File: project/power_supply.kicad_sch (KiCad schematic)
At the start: 0 parts

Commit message: Regulador V1 finalizado
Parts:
- added C1, C2, C3: 2u2, symbol Device:C
- added D1: ~, Package_TO_SOT_SMD:SOT-23, symbol Diode:MMBZxx
- added D2: LED, symbol Device:LED
- added FB1, FB2, FB3: FerriteBead_Small, symbol Device:FerriteBead_Small
- added J1: USB_C_Receptacle_USB2.0_16P, symbol Connector:USB_C_Receptacle_USB2.0_16P
- added R1, R2: 5k1, symbol Device:R
- added R3: 1k, symbol Device:R
- added TP1_5V, TP2_3V3, TP3_1V2: TestPoint, symbol Connector:TestPoint
- added U1: USBLC6-2SC6, Package_TO_SOT_SMD:SOT-23-6, symbol Power_Protection:USBLC6-2SC6
- added U2: MIC5356-S4YMME, Package_SO:MSOP-8-1EP_3x3mm_P0.65mm_EP2.5x3mm_Mask1.73x2.36mm_ThermalVias, symbol Regulator_Linear:MIC5356-S4YMME
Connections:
- new net: D1.1 (K), D1.2 (K), FB1.1, J1.A4 (VBUS), J1.A9 (VBUS), J1.B4 (VBUS), J1.B9 (VBUS), U1.5 (VBUS)
- new net: D2.2 (A), R3.2
- new net: FB3.1, U2.7 (VOUT2)
- new net: FB2.1, U2.8 (VOUT1)
- new net: J1.A5 (CC1), R1.1
- new net: J1.A6 (D+), J1.B6 (D+), U1.3 (I/O2)
- new net: J1.A7 (D-), J1.B7 (D-), U1.1 (I/O1)
- new net: J1.B5 (CC2), R2.1
- new net +1V2: C2.1, FB3.2, TP3_1V2.1
- new net +3V3: C3.1, FB2.2, TP2_3V3.1
- new net +5V: C1.1, FB1.2, R3.1, TP1_5V.1, U2.1 (VIN), U2.4 (EN2), U2.5 (EN1)
- new net D+: U1.4 (I/O2)
- new net D-: U1.6 (I/O1)
- new net GND: C1.2, C2.2, C3.2, D1.3 (A), D2.1 (K), J1.A1 (GND), J1.A12 (GND), J1.B1 (GND), J1.B12 (GND), J1.S1 (SHIELD), R1.2, R2.2, U1.2 (GND), U2.2 (GND)
- no-connect marks 0 -> 2

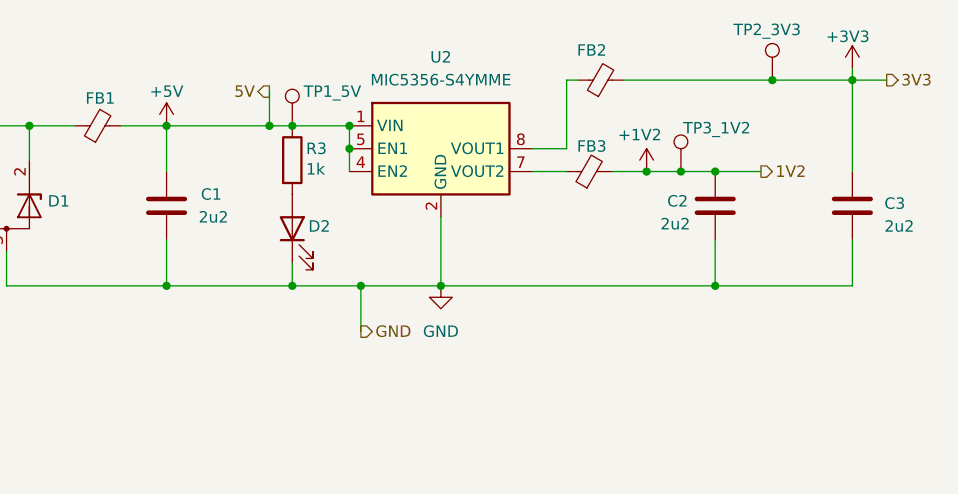
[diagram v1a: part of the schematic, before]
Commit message: Sección de FTDI casi terminada. Definir oscilador y nombres de puertos
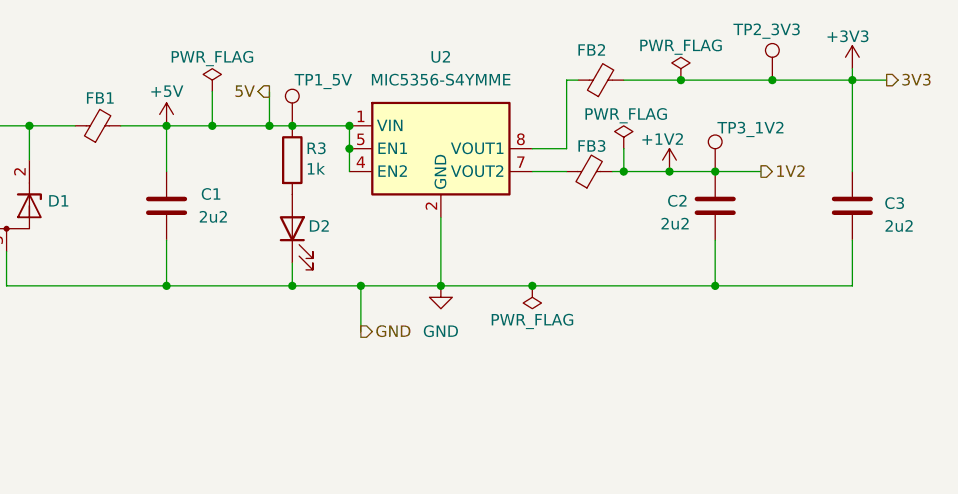
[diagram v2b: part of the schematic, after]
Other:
- moved on the sheet: TP3_1V2

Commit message: Guardado previo, FTDI casi listo
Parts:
- removed TP1_5V, TP2_3V3, TP3_1V2: TestPoint, symbol Connector:TestPoint
- removed U1: USBLC6-2SC6, Package_TO_SOT_SMD:SOT-23-6, symbol Power_Protection:USBLC6-2SC6
- removed U2: MIC5356-S4YMME, Package_SO:MSOP-8-1EP_3x3mm_P0.65mm_EP2.5x3mm_Mask1.73x2.36mm_ThermalVias, symbol Regulator_Linear:MIC5356-S4YMME
- added C4, C6, C7: 10u, symbol Device:C
- added C5: 100n, symbol Device:C
- added R4: 120, symbol Device:R
- added TP1: TP2_3V1, symbol Connector:TestPoint
- added TP2: TP1_5V1, symbol Connector:TestPoint
- added TP3: TP3_1V2, symbol Connector:TestPoint
- added TP4: TP4_GND, symbol Connector:TestPoint
- added U1: LD1117S33TR_SOT223, Package_TO_SOT_SMD:SOT-223-3_TabPin2, symbol Regulator_Linear:LD1117S33TR_SOT223
- added U2: LD1117S12TR_SOT223, Package_TO_SOT_SMD:SOT-223-3_TabPin2, symbol Regulator_Linear:LD1117S12TR_SOT223
- added U3: USBLC6-2SC6, Package_TO_SOT_SMD:SOT-23-6, symbol Power_Protection:USBLC6-2SC6
- C1: value 2u2 -> 10n
- C2: value 2u2 -> 100n
- C3: value 2u2 -> 10u
- R2: value 5k1 -> 1k
- R3: value 1k -> 5k1
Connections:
- net +1V2: now also TP3.1; no longer C2.1
- net +3V3: now also C5.1, C6.1, TP1.1, U2.3 (VI); no longer C3.1
- net +5V: now also C2.1, C3.1, R2.1, TP2.1, U1.3 (VI); no longer C1.1, R3.1
- net D+: now also U3.4 (I/O2)
- net D-: now also U3.6 (I/O1)
- net GND: now also R3.2, C4.2, C5.2, C6.2, C7.2, R4.2, TP4.1, U1.1 (GND), U2.1 (GND), U3.2 (GND); no longer R2.2
- net at D1.1 (K), D1.2 (K), FB1.1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: now also C1.1, U3.5 (VBUS)
- net at D2.2 (A): now also R2.2; no longer R3.2
- net at FB3.1: now also C7.1, R4.1, U2.2 (VO)
- net at FB2.1: now also C4.1, U1.2 (VO)
- net at J1.A6 (D+), J1.B6 (D+): now also U3.3 (I/O2)
- net at J1.A7 (D-), J1.B7 (D-): now also U3.1 (I/O1)
- net at J1.B5 (CC2): now also R3.1; no longer R2.1

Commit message: Inicio de la PCB y conexion del PLL
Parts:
- C1, C2, C3, C4, C5, C6, C7: footprint (none) -> Capacitor_SMD:C_1206_3216Metric
- D2: footprint (none) -> libraries:WL-SMTW_3528
- FB1, FB2, FB3: footprint (none) -> Diode_SMD:D_1206_3216Metric
- J1: footprint (none) -> libraries:AMPHENOL_GSB1C41110SSHR
- R1, R2, R3, R4: footprint (none) -> Resistor_SMD:R_1206_3216Metric
- TP1, TP2, TP3, TP4: footprint (none) -> TestPoint:TestPoint_Pad_D2.5mm
- U3: footprint Package_TO_SOT_SMD:SOT-23-6 -> Package_TO_SOT_SMD:SOT-666
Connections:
- net GND: no longer J1.A12 (GND), J1.B12 (GND)
- net at C1.1, D1.1 (K), D1.2 (K)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: no longer J1.A9 (VBUS), J1.B9 (VBUS)
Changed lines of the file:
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@@
 			)
 		)
-		(property "Footprint" ""
+		(property "Footprint" "Resistor_SMD:R_1206_3216Metric"
 			(at 229.362 85.09 90)
 			(effects
@@
 			)
 		)
-		(property "Footprint" ""
+		(property "Footprint" "Capacitor_SMD:C_1206_3216Metric"
 			(at 139.3952 88.9 0)
 			(effects
@@
 			)
 		)
-		(property "Footprint" ""
+		(property "Footprint" "Diode_SMD:D_1206_3216Metric"
 			(at 177.8 77.978 90)
 			(effects
@@
 			)
 		)
-		(property "Footprint" ""
+		(property "Footprint" "TestPoint:TestPoint_Pad_D2.5mm"
 			(at 154.94 73.66 0)
 			(effects
@@
 			)
 		)
-		(property "Footprint" ""
+		(property "Footprint" "libraries:AMPHENOL_GSB1C41110SSHR"
 			(at 53.34 91.44 0)
 			(effects
@@
 		(pin "B7"
 		)
-		(pin "B12"
-		)
 		(pin "B4"
 		)
@@
 		(pin "S1"
 		)
-		(pin "B9"
-		)
 		(pin "A1"
 		)
 		(pin "A8"
 		)
-		(pin "A12"
-		)
 		(pin "A4"
 		)
 		(pin "A7"
-		)
-		(pin "A9"
 		)
 		(pin "A6"
@@
 			)
 		)
-		(property "Footprint" ""
+		(property "Footprint" "Capacitor_SMD:C_1206_3216Metric"
 			(at 199.0852 88.9 0)
 			(effects
@@
 			)
 		)
-		(property "Footprint" ""
+		(property "Footprint" "Capacitor_SMD:C_1206_3216Metric"
 			(at 127.9652 88.9 0)
 			(effects
@@
 			)
 		)
-		(property "Footprint" ""
+		(property "Footprint" "TestPoint:TestPoint_Pad_D2.5mm"
 			(at 203.2 72.39 0)
 			(effects
@@
 			)
 		)
-		(property "Footprint" ""
+		(property "Footprint" "Capacitor_SMD:C_1206_3216Metric"
 			(at 183.8452 88.9 0)
 			(effects
@@
 			)
 		)
-		(property "Footprint" ""
+		(property "Footprint" "Resistor_SMD:R_1206_3216Metric"
 			(at 69.85 83.058 90)
 			(effects
@@
 			)
 		)
-		(property "Footprint" ""
+		(property "Footprint" "Diode_SMD:D_1206_3216Metric"
 			(at 120.65 77.978 90)
 			(effects
@@
 			)
 		)
-		(property "Footprint" ""
+		(property "Footprint" "Capacitor_SMD:C_1206_3216Metric"
 			(at 221.9452 88.9 0)
 			(effects
@@
 			)
 		)
-		(property "Footprint" ""
+		(property "Footprint" "libraries:WL-SMTW_3528"
 			(at 149.86 88.9 0)
 			(effects
@@
 			)
 		)
-		(property "Footprint" ""
+		(property "Footprint" "Capacitor_SMD:C_1206_3216Metric"
 			(at 173.6852 88.9 0)
 			(effects
@@
 			)
 		)
-		(property "Footprint" ""
+		(property "Footprint" "Resistor_SMD:R_1206_3216Metric"
 			(at 148.082 81.28 90)
 			(effects
@@
 			)
 		)
-		(property "Footprint" ""
+		(property "Footprint" "Capacitor_SMD:C_1206_3216Metric"
 			(at 115.2652 88.9 0)
 			(effects
@@
 			)
 		)
-		(property "Footprint" ""
+		(property "Footprint" "Resistor_SMD:R_1206_3216Metric"
 			(at 69.85 85.598 90)
 			(effects
@@
 			)
 		)
-		(property "Footprint" ""
+		(property "Footprint" "TestPoint:TestPoint_Pad_D2.5mm"
 			(at 255.27 73.66 0)
 			(effects
@@
 			)
 		)
-		(property "Footprint" "Package_TO_SOT_SMD:SOT-23-6"
+		(property "Footprint" "Package_TO_SOT_SMD:SOT-666"
 			(at 87.63 97.79 0)
 			(effects
@@
 			)
 		)
+		(property "Nombre de la hoja de datos" ""
+			(at 86.36 91.44 0)
+			(effects
+				(font
+					(size 1.27 1.27)
+				)
+				(hide yes)
+			)
+		)
+		(property "Fabricante" ""
+			(at 86.36 91.44 0)
+			(effects
+				(font
+					(size 1.27 1.27)
+				)
+				(hide yes)
+			)
+		)
+		(property "Hoja de datos del vendedor" ""
+			(at 86.36 91.44 0)
+			(effects
+				(font
+					(size 1.27 1.27)
+				)
+				(hide yes)
+			)
+		)
+		(property "Código del fabricante (Order Code)" ""
+			(at 86.36 91.44 0)
+			(effects
+				(font
+					(size 1.27 1.27)
+				)
+				(hide yes)
+			)
+		)
+		(property "Link del vendedor" ""
+			(at 86.36 91.44 0)
+			(effects
+				(font
+					(size 1.27 1.27)
+				)
+				(hide yes)
+			)
+		)
+		(property "Código del vendedor (Provider Order Code)" ""
+			(at 86.36 91.44 0)
+			(effects
+				(font
+					(size 1.27 1.27)
+				)
+				(hide yes)
+			)
+		)
+		(property "Tecnología" ""
+			(at 86.36 91.44 0)
+			(effects
+				(font
+					(size 1.27 1.27)
+				)
+				(hide yes)
+			)
+		)
 		(pin "4"
 		)
@@
 			)
 		)
-		(property "Footprint" ""
+		(property "Footprint" "Diode_SMD:D_1206_3216Metric"
 			(at 236.22 77.978 90)
 			(effects
@@
 			)
 		)
-		(property "Footprint" ""
+		(property "Footprint" "TestPoint:TestPoint_Pad_D2.5mm"
 			(at 167.64 95.25 0)
 			(effects

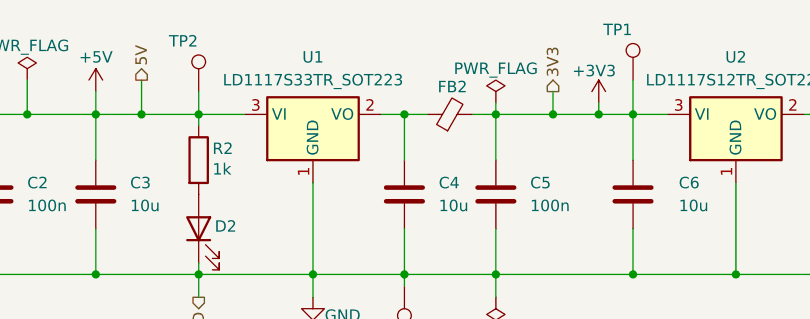
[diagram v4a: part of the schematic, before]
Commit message: Eliminación de archivos de respaldo y correcciones en la biblioteca de componentes. Se eliminaron archivos de autosave, archivos de esquemas y modelos 3D no utilizados, así como modificaciones en las propiedades de algunos componentes en la biblioteca.
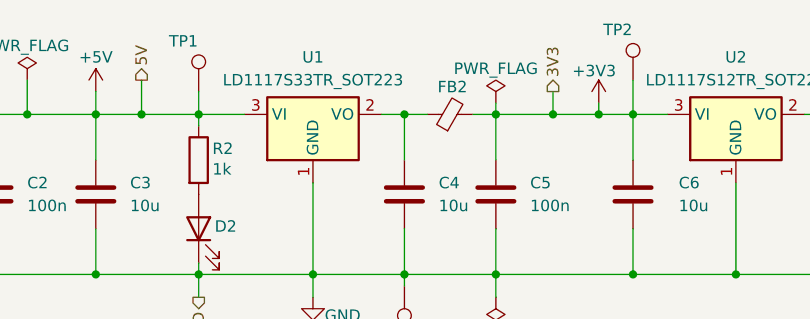
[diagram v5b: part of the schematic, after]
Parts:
- U3: footprint Package_TO_SOT_SMD:SOT-666 -> Package_TO_SOT_SMD:SOT-23-6
- renumbered TP2 to TP1, TP1 to TP2
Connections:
- net GND: now also J1.A12 (GND), J1.B12 (GND)
- net at C1.1, D1.1 (K), D1.2 (K)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: now also J1.A9 (VBUS), J1.B9 (VBUS)
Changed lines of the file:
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@@
 		(on_board yes)
 		(dnp no)
-		(property "Reference" "TP2"
+		(property "Reference" "TP1"
 			(at 146.558 68.072 0)
 			(effects
@@
 			(project "fpga-utn"
 				(path "/fadb8841-cd7a-4174-937d-7c393e857c90/addbb95a-5ecf-43db-ab5f-45b593a9e920"
-					(reference "TP2")
+					(reference "TP1")
 					(unit 1)
 				)
@@
 		(pin "B1"
 		)
+		(pin "A12"
+		)
+		(pin "A9"
+		)
+		(pin "B12"
+		)
+		(pin "B9"
+		)
 		(instances
 			(project "fpga-utn"
@@
 		(on_board yes)
 		(dnp no)
-		(property "Reference" "TP1"
+		(property "Reference" "TP2"
 			(at 194.818 66.802 0)
 			(effects
@@
 			(project "fpga-utn"
 				(path "/fadb8841-cd7a-4174-937d-7c393e857c90/addbb95a-5ecf-43db-ab5f-45b593a9e920"
-					(reference "TP1")
+					(reference "TP2")
 					(unit 1)
 				)
@@
 			)
 		)
-		(property "Footprint" "Package_TO_SOT_SMD:SOT-666"
+		(property "Footprint" "Package_TO_SOT_SMD:SOT-23-6"
 			(at 87.63 97.79 0)
 			(effects

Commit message: - Included properties such as Reference, Value, Footprint, and various manufacturer details. - Defined 20 pins with appropriate names and attributes for the symbol. - Ensured compatibility with KiCad version 8.0 and above.
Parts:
- FB1, FB2, FB3: footprint Diode_SMD:D_1206_3216Metric -> (none)

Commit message: Agregados footprints de todos los componentes
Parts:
- D2: value LED -> LED Green; footprint libraries:WL-SMTW_3528 -> 150141RS73100(LED):LEDM3528X210N
- FB1, FB2, FB3: footprint (none) -> Inductor_SMD:L_1206_3216Metric_Pad1.42x1.75mm_HandSolder
- J1: footprint libraries:AMPHENOL_GSB1C41110SSHR -> GSB1C41110SSHR:GSB1C41110SSHR
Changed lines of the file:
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@@
 			)
 		)
-		(property "Footprint" ""
+		(property "Footprint" "Inductor_SMD:L_1206_3216Metric_Pad1.42x1.75mm_HandSolder"
 			(at 177.8 77.978 90)
 			(effects
@@
 			)
 		)
-		(property "Footprint" "libraries:AMPHENOL_GSB1C41110SSHR"
+		(property "Footprint" "GSB1C41110SSHR:GSB1C41110SSHR"
 			(at 53.34 91.44 0)
 			(effects
@@
 			)
 		)
+		(property "Nombre de la hoja de datos" ""
+			(at 49.53 91.44 0)
+			(effects
+				(font
+					(size 1.27 1.27)
+				)
+				(hide yes)
+			)
+		)
+		(property "Fabricante" ""
+			(at 49.53 91.44 0)
+			(effects
+				(font
+					(size 1.27 1.27)
+				)
+				(hide yes)
+			)
+		)
+		(property "Hoja de datos del vendedor" ""
+			(at 49.53 91.44 0)
+			(effects
+				(font
+					(size 1.27 1.27)
+				)
+				(hide yes)
+			)
+		)
+		(property "Código del fabricante (Order Code)" ""
+			(at 49.53 91.44 0)
+			(effects
+				(font
+					(size 1.27 1.27)
+				)
+				(hide yes)
+			)
+		)
+		(property "Link del vendedor" ""
+			(at 49.53 91.44 0)
+			(effects
+				(font
+					(size 1.27 1.27)
+				)
+				(hide yes)
+			)
+		)
+		(property "Código del vendedor (Provider Order Code)" ""
+			(at 49.53 91.44 0)
+			(effects
+				(font
+					(size 1.27 1.27)
+				)
+				(hide yes)
+			)
+		)
+		(property "Tecnología" ""
+			(at 49.53 91.44 0)
+			(effects
+				(font
+					(size 1.27 1.27)
+				)
+				(hide yes)
+			)
+		)
 		(pin "B5"
 		)
@@
 			)
 		)
-		(property "Footprint" ""
+		(property "Footprint" "Inductor_SMD:L_1206_3216Metric_Pad1.42x1.75mm_HandSolder"
 			(at 120.65 77.978 90)
 			(effects
@@
 			)
 		)
-		(property "Value" "LED"
+		(property "Value" "LED Green"
 			(at 152.654 90.424 90)
 			(effects
@@
 			)
 		)
-		(property "Footprint" "libraries:WL-SMTW_3528"
+		(property "Footprint" "150141RS73100(LED):LEDM3528X210N"
 			(at 149.86 88.9 0)
 			(effects
@@
 			)
 		)
-		(property "Footprint" ""
+		(property "Footprint" "Inductor_SMD:L_1206_3216Metric_Pad1.42x1.75mm_HandSolder"
 			(at 236.22 77.978 90)
 			(effects

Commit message: PCB etapa de potencia y comunicacion lista
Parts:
- removed TP1: TP1_5V1, TestPoint:TestPoint_Pad_D2.5mm, symbol Connector:TestPoint
- removed TP2: TP2_3V1, TestPoint:TestPoint_Pad_D2.5mm, symbol Connector:TestPoint
- removed TP3: TP3_1V2, TestPoint:TestPoint_Pad_D2.5mm, symbol Connector:TestPoint
- removed TP4: TP4_GND, TestPoint:TestPoint_Pad_D2.5mm, symbol Connector:TestPoint
